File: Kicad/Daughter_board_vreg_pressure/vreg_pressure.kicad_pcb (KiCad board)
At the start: 2 copper layers, 0 parts

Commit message: pcb finalized
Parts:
- added C1: 10uF, Capacitors_SMD:C_0402, F.Cu at (149.1, 97.0)
- added C2: 2.2uF, Capacitors_SMD:C_0402, F.Cu at (157.7, 90.7)
- added C3: 0.1uF, Capacitors_SMD:C_0402, F.Cu at (140.0, 106.4)
- added C4: 10uF, Capacitors_SMD:C_0402, F.Cu at (144.0, 107.7)
- added C5: 0.1uF, Capacitors_SMD:C_0402, F.Cu at (142.2, 107.7)
- added IC1: SPX1117M3, custom:SPX1117M3, F.Cu at (150.4, 93.7)
- added J1: BATT, custom:BATT_CONN, F.Cu at (156.7, 85.9)
- added U1: MPL3115A2, custom:MPL3115A2, F.Cu at (134.9, 108.2)
- added VIA_HOME_ETCH: VAL**, custom:VIA_HOME_ETCH, F.Cu at (158.0, 94.0)
- added VIA_HOME_ETCH: VAL**, custom:VIA_HOME_ETCH, F.Cu at (143.5, 104.0)
- added conn1: I2C_CONN, custom:I2C_CONN, F.Cu at (139.1, 99.9)
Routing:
- net 3V3: track 0.00 -> 51.0 mm
- net GND: track 0.00 -> 40.9 mm
- net Net-(U1-Pad8): track 0.00 -> 16.0 mm
- net Net-(C2-Pad1): track 0.00 -> 11.3 mm
- net Net-(U1-Pad7): track 0.00 -> 8.85 mm
- net Net-(C3-Pad1): track 0.00 -> 3.09 mm
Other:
- board outline added: 31 x 29 mm
- board text added: "+"
- board text added: "-"
- board text added: "C1"
- board text added: "C4"
- board text added: "C5"
- board text added: "IC1"
- board text added: "WeatherSpot"

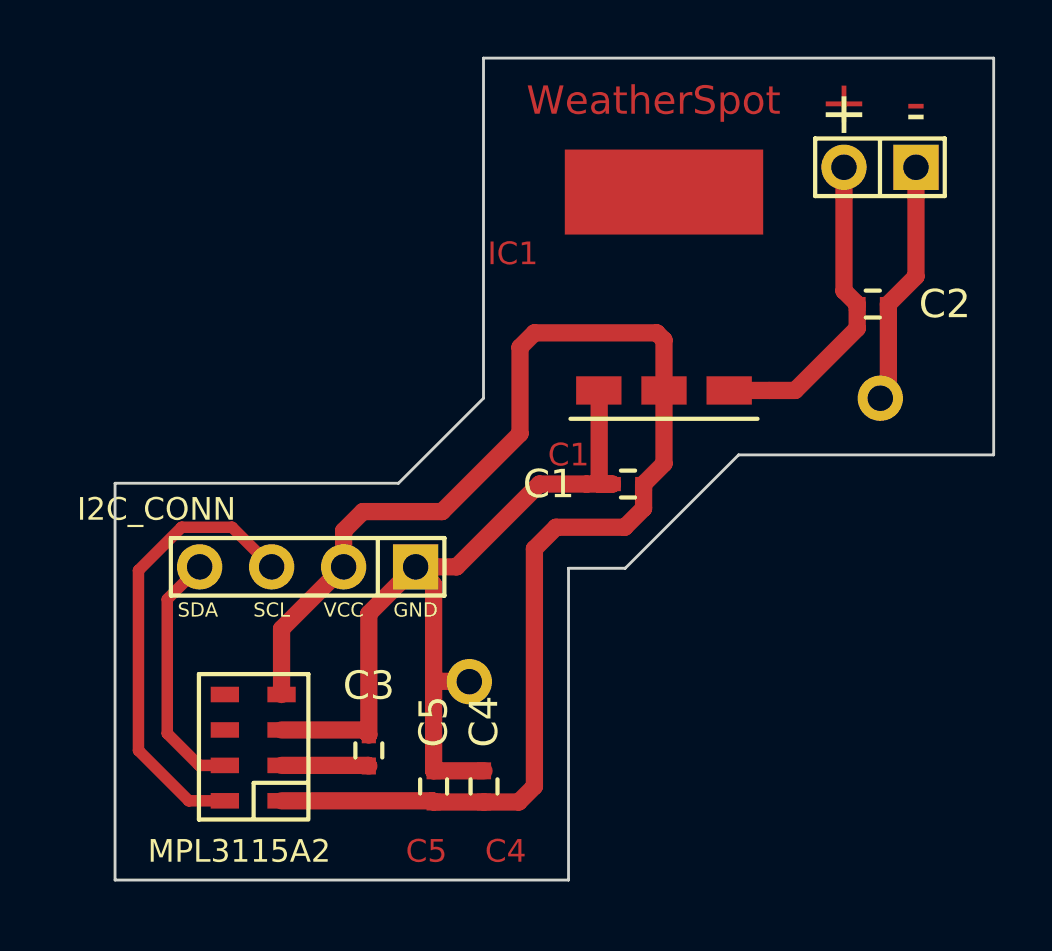
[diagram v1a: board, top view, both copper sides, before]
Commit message: removed the vreg and left the pressure sensor.
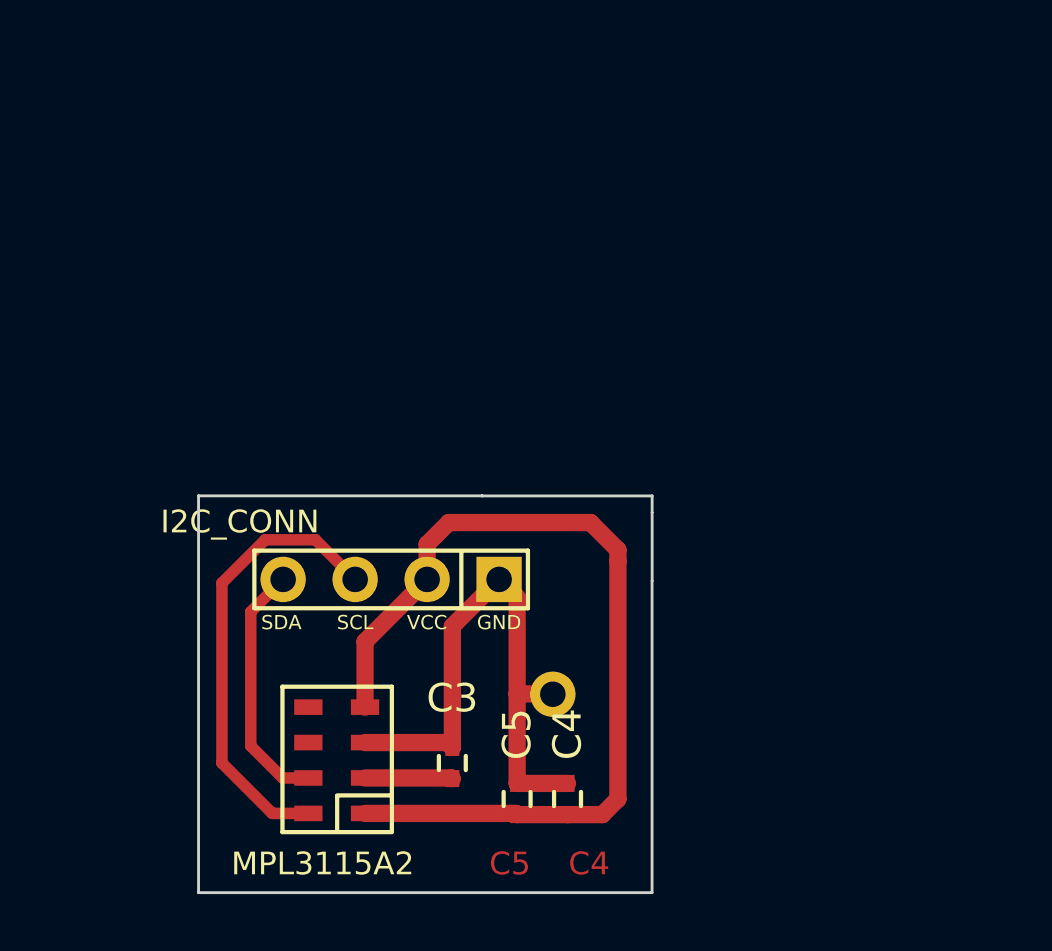
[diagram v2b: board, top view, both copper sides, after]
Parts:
- removed C1: 10uF, Capacitors_SMD:C_0402
- removed C2: 2.2uF, Capacitors_SMD:C_0402
- removed IC1: SPX1117M3, custom:SPX1117M3
- removed J1: BATT, custom:BATT_CONN
- removed the VIA_HOME_ETCH at (158.0, 94.0)
- moved C4 2.98 mm to (147.0, 108.1)
- moved U1 2.98 mm to (137.8, 108.6)
- moved VIA_HOME_ETCH 2.98 mm to (146.4, 104.4)
- moved conn1 2.98 mm to (142.0, 100.4)
- moved C3 2.98 mm to (142.9, 106.9)
- moved C5 2.98 mm to (145.2, 108.1)
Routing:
- net GND: track 40.9 -> 20.3 mm
- net 3V3: track 51.0 -> 32.1 mm
- net Net-(C2-Pad1): track 11.3 -> 0.00 mm
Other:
- board size 31 x 29 mm -> 16 x 14 mm
- board text removed: "+"
- board text removed: "-"
- board text removed: "C1"
- board text removed: "IC1"
- board text removed: "WeatherSpot"
